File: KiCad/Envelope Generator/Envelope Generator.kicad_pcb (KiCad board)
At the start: 2 copper layers, 78 x 57 mm, 64 parts, among them J1 Screw_Terminal_01x03, J2 Screw_Terminal_01x03, U1 TL074, U2 TL074, U3 TL074

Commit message: added silkscreen to help assembly process on all boards
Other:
- board text added: "100k"
- board text added: "10k"
- board text added: "200k"
- board text added: "50k"
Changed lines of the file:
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@@
 		)
 		(property "Value" "1u"
-			(at 2.5 3.5 0)
-			(layer "F.Fab")
+			(at 2.5 0 0)
+			(layer "F.SilkS")
 			(effects
 				(font
@@
 		)
 		(property "Value" "1u"
-			(at 2.5 3.5 90)
-			(layer "F.Fab")
+			(at 2.5 0 180)
+			(layer "F.SilkS")
 			(effects
 				(font
@@
 		)
 		(property "Value" "TL074"
-			(at 3.81 17.57 0)
-			(layer "F.Fab")
+			(at 3.81 7.62 0)
+			(layer "F.SilkS")
 			(effects
 				(font
@@
 		)
 		(property "Value" "TL074"
-			(at 3.81 17.57 0)
-			(layer "F.Fab")
+			(at 3.81 7.62 0)
+			(layer "F.SilkS")
 			(effects
 				(font
@@
 		)
 		(property "Value" "TL074"
-			(at 3.81 17.57 90)
-			(layer "F.Fab")
+			(at 3.81 7.7 180)
+			(layer "F.SilkS")
 			(effects
 				(font
@@
 		)
 		(property "Value" "1u"
-			(at 2.5 3.5 90)
-			(layer "F.Fab")
+			(at 2.5 0 180)
+			(layer "F.SilkS")
 			(effects
 				(font
@@
 		)
 		(property "Value" "1u"
-			(at 2.5 3.5 0)
-			(layer "F.Fab")
+			(at 2.5 0 0)
+			(layer "F.SilkS")
 			(effects
 				(font
@@
 		(layer "Edge.Cuts")
 	)
+	(gr_text "100k"
+		(at 20 92.5 0)
+		(layer "F.SilkS")
+		(effects
+			(font
+				(size 1 1)
+				(thickness 0.15)
+			)
+		)
+	)
+	(gr_text "200k"
+		(at 21 72 0)
+		(layer "F.SilkS")
+		(effects
+			(font
+				(size 1 1)
+				(thickness 0.15)
+			)
+		)
+	)
+	(gr_text "10k"
+		(at 30 72 0)
+		(layer "F.SilkS")
+		(effects
+			(font
+				(size 1 1)
+				(thickness 0.15)
+			)
+		)
+	)
+	(gr_text "200k"
+		(at 39 72 0)
+		(layer "F.SilkS")
+		(effects
+			(font
+				(size 1 1)
+				(thickness 0.15)
+			)
+		)
+	)
+	(gr_text "100k"
+		(at 39 80.5 0)
+		(layer "F.SilkS")
+		(effects
+			(font
+				(size 1 1)
+				(thickness 0.15)
+			)
+		)
+	)
+	(gr_text "100k"
+		(at 39 93 0)
+		(layer "F.SilkS")
+		(effects
+			(font
+				(size 1 1)
+				(thickness 0.15)
+			)
+		)
+	)
+	(gr_text "200k"
+		(at 48 72 0)
+		(layer "F.SilkS")
+		(effects
+			(font
+				(size 1 1)
+				(thickness 0.15)
+			)
+		)
+	)
+	(gr_text "200k"
+		(at 58 72 0)
+		(layer "F.SilkS")
+		(effects
+			(font
+				(size 1 1)
+				(thickness 0.15)
+			)
+		)
+	)
+	(gr_text "100k"
+		(at 64.5 102 0)
+		(layer "F.SilkS")
+		(effects
+			(font
+				(size 1 1)
+				(thickness 0.15)
+			)
+		)
+	)
+	(gr_text "200k"
+		(at 67 72 0)
+		(layer "F.SilkS")
+		(effects
+			(font
+				(size 1 1)
+				(thickness 0.15)
+			)
+		)
+	)
+	(gr_text "100k"
+		(at 67 81 0)
+		(layer "F.SilkS")
+		(effects
+			(font
+				(size 1 1)
+				(thickness 0.15)
+			)
+		)
+	)
+	(gr_text "100k"
+		(at 67 93 0)
+		(layer "F.SilkS")
+		(effects
+			(font
+				(size 1 1)
+				(thickness 0.15)
+			)
+		)
+	)
+	(gr_text "50k"
+		(at 76 72 0)
+		(layer "F.SilkS")
+		(effects
+			(font
+				(size 1 1)
+				(thickness 0.15)
+			)
+		)
+	)
+	(gr_text "200k"
+		(at 85 72 0)
+		(layer "F.SilkS")
+		(effects
+			(font
+				(size 1 1)
+				(thickness 0.15)
+			)
+		)
+	)
+	(gr_text "100k"
+		(at 86 93 0)
+		(layer "F.SilkS")
+		(effects
+			(font
+				(size 1 1)
+				(thickness 0.15)
+			)
+		)
+	)
 	(gr_text "Sus\nV"

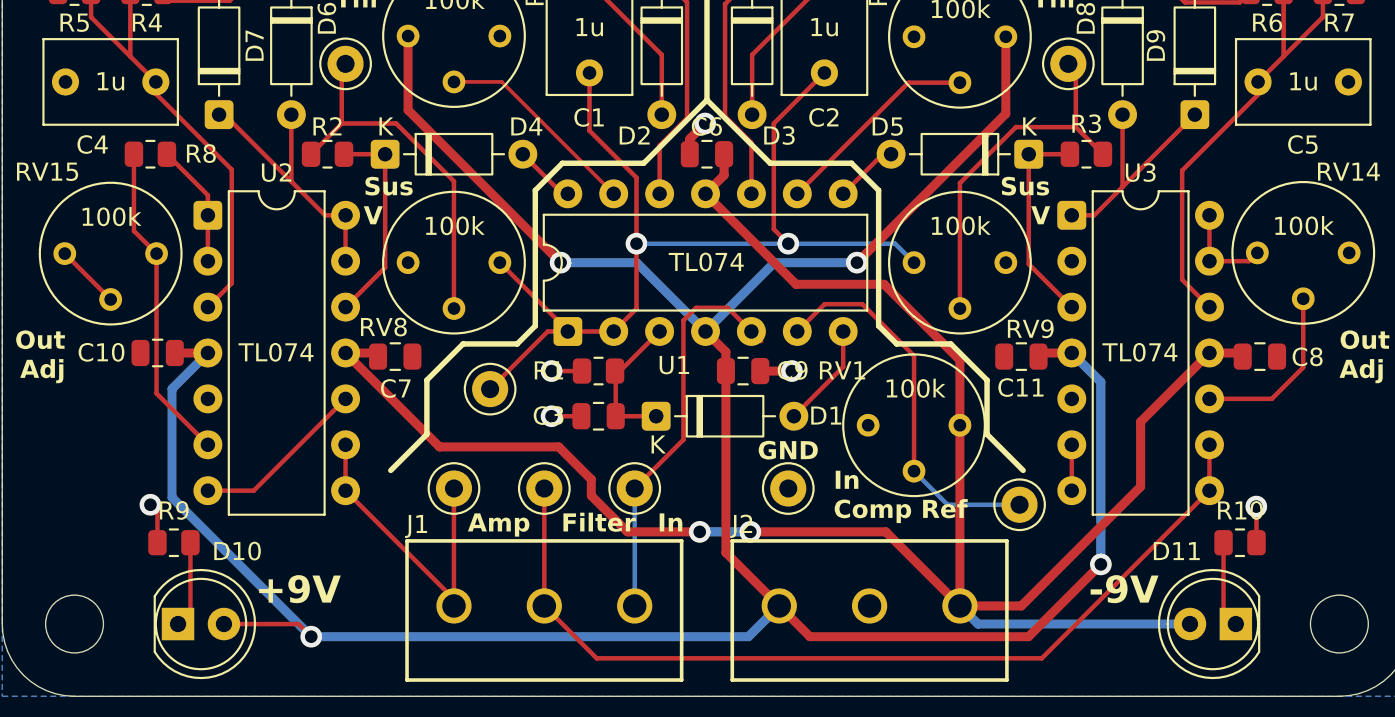
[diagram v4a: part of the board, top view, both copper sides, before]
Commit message: ran DRC on all boards
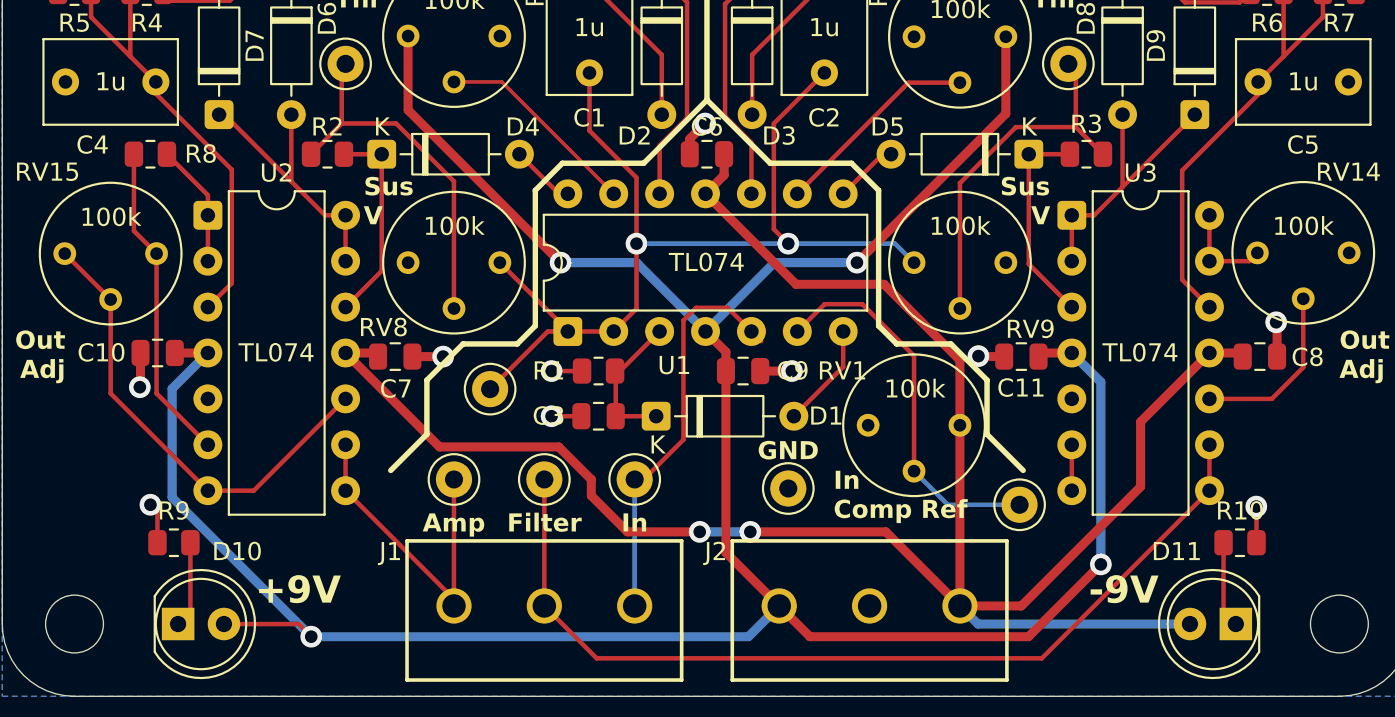
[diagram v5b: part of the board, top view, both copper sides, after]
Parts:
- moved TP7 0.50 mm to (39.0, 107.0)
- moved TP8 0.50 mm to (44.0, 107.0)
- moved TP9 0.50 mm to (49.0, 107.0)
- moved D4 0.19 mm to (35.0, 89.0)
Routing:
- net Net-(U2C-+): track 13.3 -> 26.1 mm
- net GND: track 11.4 -> 18.4 mm, vias 6 -> 10
- net /Envelope Generator/Filter Target Voltage: track 13.1 -> 15.7 mm
- net /Envelope Generator/Amp Out: track 18.1 -> 19.1 mm
- net /Envelope Generator/Filter Out: track 50.9 -> 51.4 mm
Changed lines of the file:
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@@
 		(at 44 114)
 		(property "Reference" "J1"
-			(at -7 -4.5 0)
+			(at -8.5 -3 0)
 			(layer "F.SilkS")
 			(effects
@@
 	(footprint "Diode_THT:D_DO-35_SOD27_P7.62mm_Horizontal"
 		(layer "F.Cu")
-		(at 35.19 89)
+		(at 35 89)
 		(descr "Diode, DO-35_SOD27 series, Axial, Horizontal, pin pitch=7.62mm, length*diameter=4*2mm^2, http://www.diodes.com/_files/packages/DO-35.pdf")
 		(tags "Diode DO-35_SOD27 series Axial Horizontal pin pitch 7.62mm  length 4mm diameter 2mm")
@@
 	(footprint "TestPoint:TestPoint_Keystone_5000-5004_Miniature"
 		(layer "F.Cu")
-		(at 44 107.5)
+		(at 44 107)
 		(descr "Keystone THM Miniature Test Point 5000-5004, http://www.keyelco.com/product-pdf.cfm?p=1309")
 		(tags "Through Hole Mount Test Points")
@@
 		(at 62 114)
 		(property "Reference" "J2"
-			(at -7 -4.5 0)
+			(at -8.5 -3 0)
 			(layer "F.SilkS")
 			(effects
@@
 	(footprint "TestPoint:TestPoint_Keystone_5000-5004_Miniature"
 		(layer "F.Cu")
-		(at 39 107.5)
+		(at 39 107)
 		(descr "Keystone THM Miniature Test Point 5000-5004, http://www.keyelco.com/product-pdf.cfm?p=1309")
 		(tags "Through Hole Mount Test Points")
@@
 	(footprint "TestPoint:TestPoint_Keystone_5000-5004_Miniature"
 		(layer "F.Cu")
-		(at 49 107.5)
+		(at 49 107)
 		(descr "Keystone THM Miniature Test Point 5000-5004, http://www.keyelco.com/product-pdf.cfm?p=1309")
 		(tags "Through Hole Mount Test Points")
@@
 	)
 	(gr_text "Amp"
-		(at 41.5 110 0)
+		(at 39 110 0)
 		(layer "F.SilkS")
 		(effects
@@
 	)
 	(gr_text "Filter"
-		(at 47 110 0)
+		(at 44 110 0)
 		(layer "F.SilkS")
 		(effects
@@
 	)
 	(gr_text "In"
-		(at 51 110 0)
+		(at 49 110 0)
 		(layer "F.SilkS")
 		(effects
@@
 	)
 	(segment
+		(start 36.7 100.2)
+		(end 38.4 100.2)
+		(width 0.5)
+		(layer "F.Cu")
+		(net "GND")
+	)
+	(segment
 		(start 52.05 89)
 		(end 52.05 88.15)
@@
 	)
 	(segment
+		(start 21.65 100)
+		(end 21.65 101.857947)
+		(width 0.5)
+		(layer "F.Cu")
+		(net "GND")
+	)
+	(segment
 		(start 83.4125 110.5)
 		(end 83.4125 108.5125)
@@
 	)
 	(segment
+		(start 84.5 98.6)
+		(end 84.55 98.65)
+		(width 0.5)
+		(layer "F.Cu")
+		(net "GND")
+	)
+	(segment
+		(start 84.55 98.65)
+		(end 84.55 100.2)
+		(width 0.5)
+		(layer "F.Cu")
+		(net "GND")
+	)
+	(segment
 		(start 22.5875 108.7875)
 		(end 22.2 108.4)
@@
 	)
 	(segment
+		(start 69.45 100.2)
+		(end 68.052774 100.2)
+		(width 0.5)
+		(layer "F.Cu")
+		(net "GND")
+	)
+	(segment
 		(start 55.95 101)
 		(end 57.7 101)
@@
 	)
 	(segment
+		(start 68.052774 100.2)
+		(end 68.024997 100.172223)
+		(width 0.5)
+		(layer "F.Cu")
+		(net "GND")
+	)
+	(segment
 		(start 52.05 88.15)
 		(end 52.9 87.3)
@@
 	)
 	(segment
+		(start 84.5 98.3)
+		(end 84.5 98.6)
+		(width 0.5)
+		(layer "F.Cu")
+		(net "GND")
+	)
+	(segment
 		(start 83.4125 108.5125)
 		(end 83.4 108.5)
@@
 		(net "GND")
 	)
+	(segment
+		(start 21.65 101.857947)
+		(end 21.615 101.892947)
+		(width 0.5)
+		(layer "F.Cu")
+		(net "GND")
+	)
 	(via
 		(at 52.9 87.3)
@@
 	)
 	(via
+		(at 84.5 98.3)
+		(size 1.2)
+		(drill 0.7)
+		(layers "F.Cu" "B.Cu")
+		(net "GND")
+	)
+	(via
 		(at 44.4 103.5)
 		(size 1.2)
@@
 	)
 	(via
+		(at 21.615 101.892947)
+		(size 1.2)
+		(drill 0.7)
+		(layers "F.Cu" "B.Cu")
+		(net "GND")
+	)
+	(via
+		(at 68.024997 100.172223)
+		(size 1.2)
+		(drill 0.7)
+		(layers "F.Cu" "B.Cu")
+		(net "GND")
+	)
+	(via
 		(at 83.4 108.5)
 		(size 1.2)
@@
 		(net "GND")
 	)
+	(via
+		(at 38.4 100.2)
+		(size 1.2)
+		(drill 0.7)
+		(layers "F.Cu" "B.Cu")
+		(net "GND")
+	)
 	(segment
 		(start 83.5 85.7)
@@
 	)
 	(segment
+		(start 20 102.24)
+		(end 25.38 107.62)
+		(width 0.25)
+		(layer "F.Cu")
+		(net "Net-(U2C-+)")
+	)
+	(segment
+		(start 20 97.04)
+		(end 20 102.24)
+		(width 0.25)
+		(layer "F.Cu")
+		(net "Net-(U2C-+)")
+	)
+	(segment
 		(start 25.38 107.62)
 		(end 27.92 107.62)
@@
 	)
 	(segment
+		(start 39 107.5)
+		(end 39 107)
+		(width 0.25)
+		(layer "F.Cu")
+		(net "/Envelope Generator/Amp Out")
+	)
+	(segment
 		(start 33 107.62)
 		(end 39 113.62)
@@
 	)
 	(segment
-		(start 33 105.08)
-		(end 33 107.62)
+		(start 39 107)
+		(end 39 114)
 		(width 0.25)
 		(layer "F.Cu")
@@
 	)
 	(segment
-		(start 39 113.62)
-		(end 39 114)
+		(start 33 105.08)
+		(end 33 107.62)
 		(width 0.25)
 		(layer "F.Cu")
@@
 	)
 	(segment
-		(start 39 107.5)
+		(start 39 113.62)
 		(end 39 114)
 		(width 0.25)
@@
 	(segment
 		(start 44 114)
-		(end 44 107.5)
+		(end 44 107)
 		(width 0.25)
 		(layer "F.Cu")
@@
 	)
 	(segment
-		(start 51.7 104.8)
-		(end 49 107.5)
+		(start 54.15 97.5)
+		(end 52.4 97.5)
 		(width 0.25)
 		(layer "F.Cu")
@@
 	)
 	(segment
-		(start 55.46 98.81)
-		(end 54.15 97.5)
+		(start 52.4 97.5)
+		(end 51.7 98.2)
 		(width 0.25)
 		(layer "F.Cu")
@@
 	)
 	(segment
-		(start 51.7 98.2)
-		(end 51.7 104.8)
+		(start 49.5 107)
+		(end 49 107)
 		(width 0.25)
 		(layer "F.Cu")
@@
 	)
 	(segment
-		(start 54.15 97.5)
-		(end 52.4 97.5)
+		(start 51.7 104.8)
+		(end 49.5 107)
 		(width 0.25)
 		(layer "F.Cu")
@@
 	)
 	(segment
-		(start 52.4 97.5)
-		(end 51.7 98.2)
+		(start 51.7 98.2)
+		(end 51.7 104.8)
 		(width 0.25)
 		(layer "F.Cu")
@@
 	)
 	(segment
-		(start 49 107.5)
+		(start 55.46 98.81)
+		(end 54.15 97.5)
+		(width 0.25)
+		(layer "F.Cu")
+		(net "/Envelope Generator/In")
+	)
+	(segment
+		(start 49 107)
 		(end 49 114)
 		(width 0.25)
@@
 	)
 	(segment
-		(start 35.19 89)
+		(start 35 89)
 		(end 32.9125 89)
 		(width 0.25)
@@
 	)
 	(segment
-		(start 35.19 89)
-		(end 35.19 95.27)
+		(start 35 95.46)
+		(end 33 97.46)
 		(width 0.25)
 		(layer "F.Cu")
@@
 	)
 	(segment
-		(start 35.19 95.27)
-		(end 33 97.46)
+		(start 35 89)
+		(end 35 95.46)
 		(width 0.25)
 		(layer "F.Cu")
@@
 	)
 	(segment
+		(start 73.19 92.38)
+		(end 73.19 94.92)
+		(width 0.25)
+		(layer "F.Cu")
+		(net "/Envelope Generator/Filter Target Voltage")
+	)
+	(segment
 		(start 80.81 100)
 		(end 82.55 100)
@@
 	)
 	(segment
-		(start 45 91.19)
-		(end 45.3 91.19)
+		(start 42.62 89)
+		(end 44.81 91.19)
 		(width 0.25)
 		(layer "F.Cu")
@@
 	)
 	(segment
-		(start 42.81 89)
-		(end 45 91.19)
+		(start 44.81 91.19)
+		(end 45.3 91.19)
 		(width 0.25)
 		(layer "F.Cu")
